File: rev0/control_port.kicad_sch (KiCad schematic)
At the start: 26 parts, among them IC1 ECP5-BGA256, U16 TC7USB42MU, U8 USB3343-CP

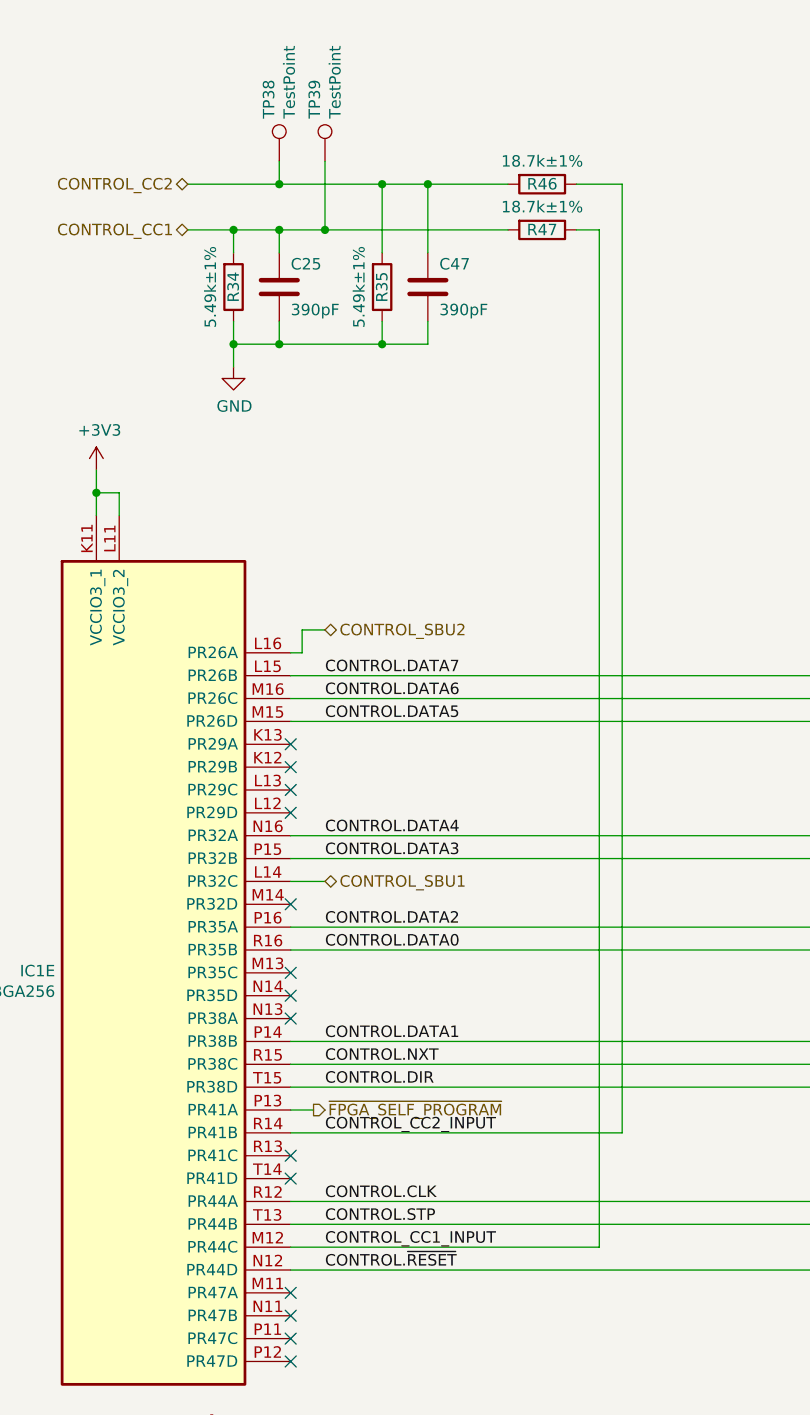
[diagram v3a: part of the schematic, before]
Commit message: hardware: simplify Control port Type-C connections
- remove CC/FPGA connections to ensure correct Rd is reliably present
- remove SBU/FPGA connections to avoid need for ESD protection

We provide CC and SBU pin access on the Target and Aux port. They are
not necessary on the Control port. Simplification ensures reliability.
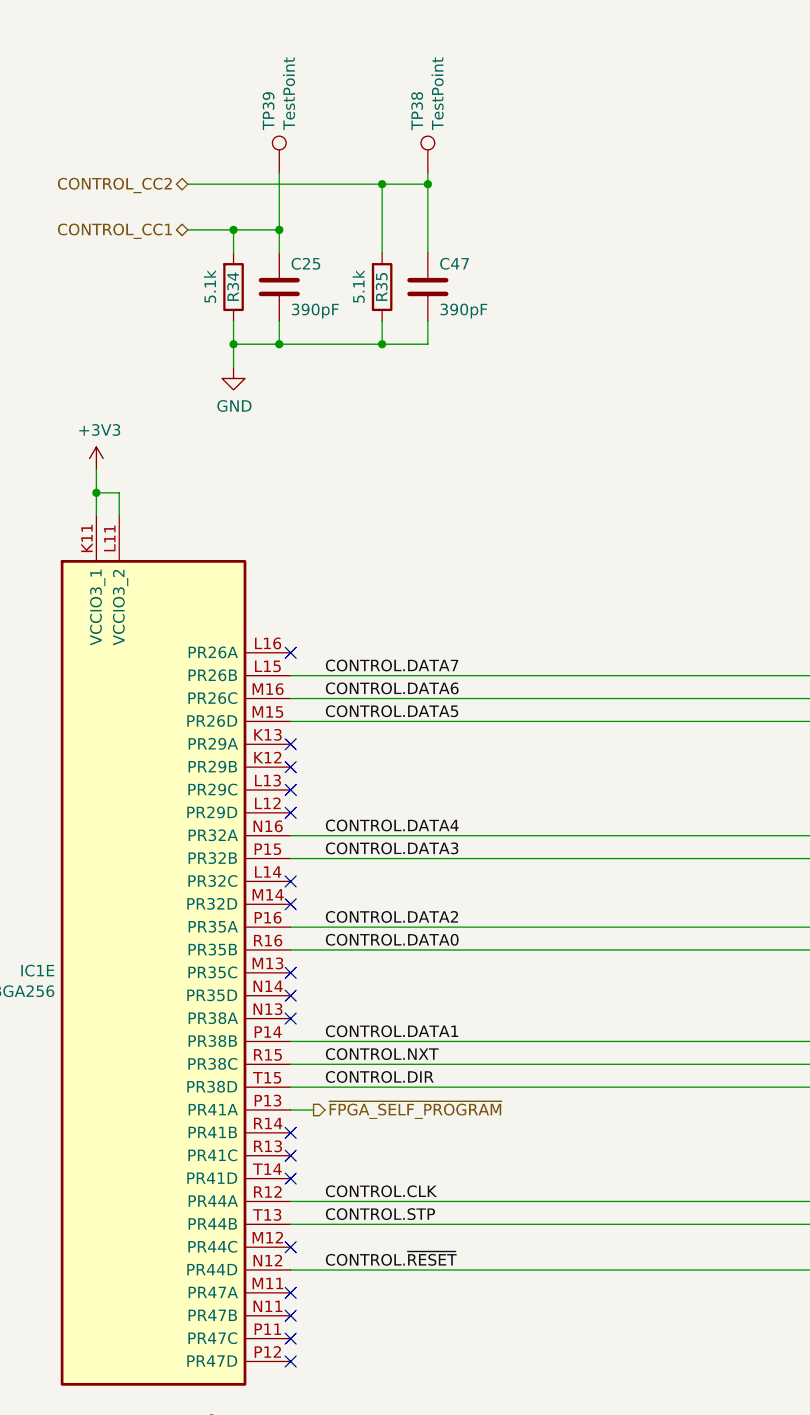
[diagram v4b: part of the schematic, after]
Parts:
- removed R46, R47: 18.7k±1%, Resistor_SMD:R_0402_1005Metric, symbol Device:R
- R34, R35: value 5.49k±1% -> 5.1k; Manufacturer Panasonic -> Yageo; Part Number ERJ-2RKF5491X -> RC0402JR-075K1L
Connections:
- net CONTROL_CC1_INPUT: no longer names the net of IC1.M12 (PR44C)
- net CONTROL_CC2_INPUT: no longer names the net of IC1.R14 (PR41B)
- net CONTROL_SBU1: no longer names the net of IC1.L14 (PR32C)
- net CONTROL_SBU2: no longer names the net of IC1.L16 (PR26A)
- no-connect marks 15 -> 19
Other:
- moved on the sheet: TP38, TP39

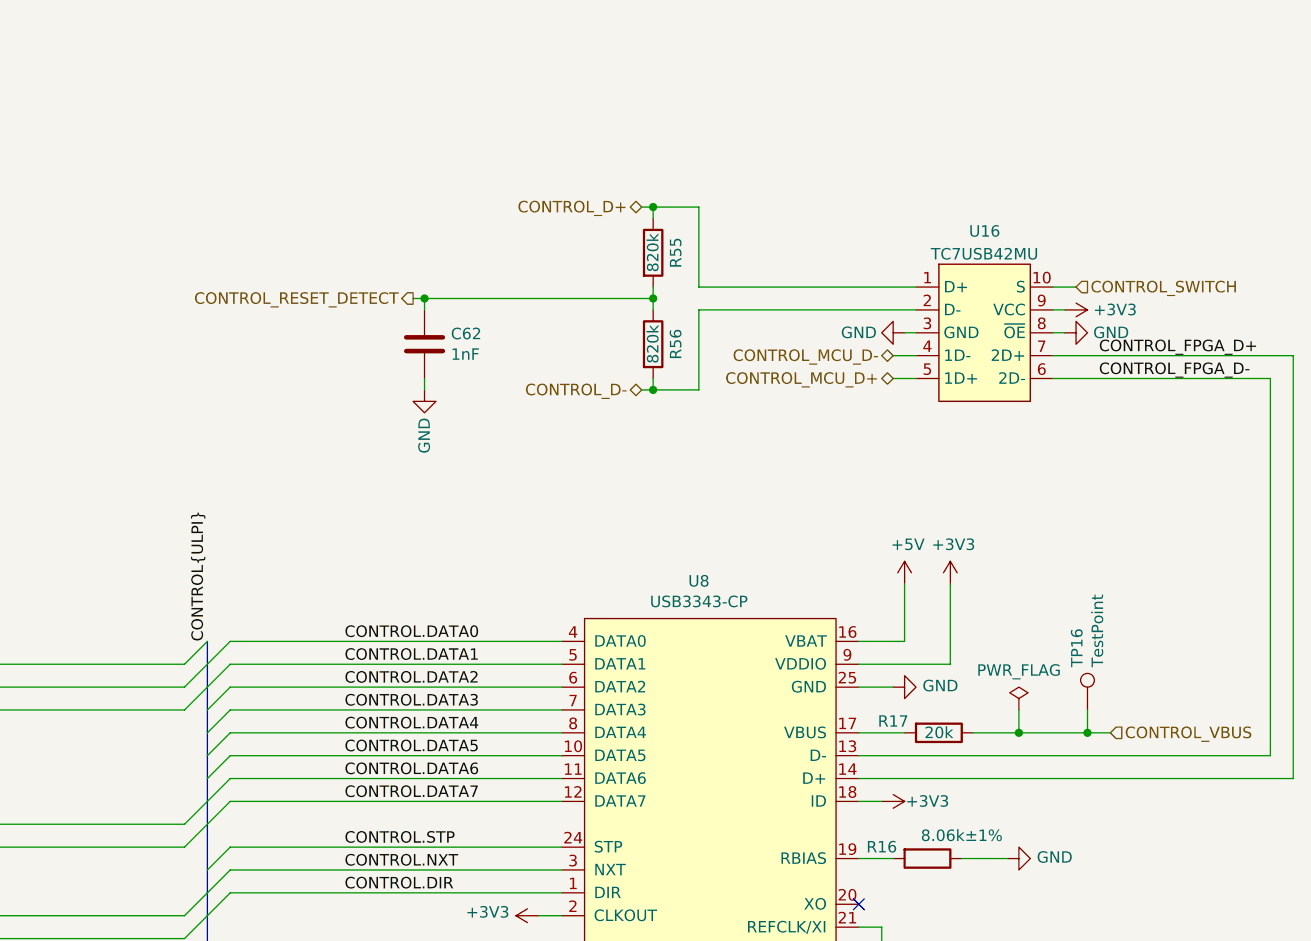
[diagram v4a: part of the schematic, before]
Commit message: hardware: clamp VBUS detection signals to 24 V
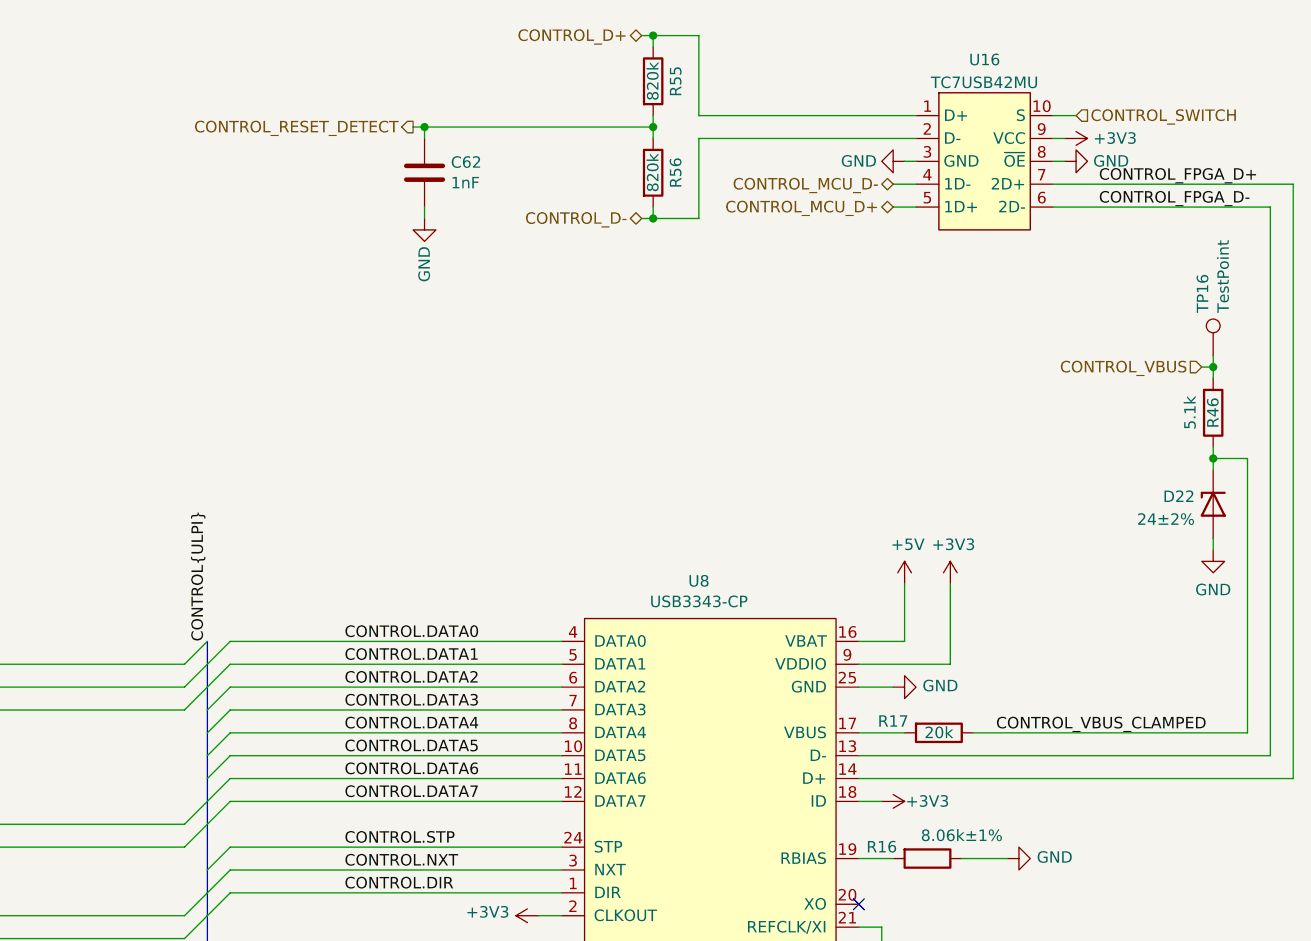
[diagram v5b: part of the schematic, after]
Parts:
- added D22: 24±2%, luna:DFN1006-2, symbol Device:D_Zener
- added R46: 5.1k, Resistor_SMD:R_0402_1005Metric, symbol Device:R
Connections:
- net CONTROL_VBUS: now also R46.2; no longer R17.1
- net GND: now also D22.2 (A)
- new net CONTROL_VBUS_CLAMPED: D22.1 (K), R17.1, R46.1
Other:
- moved on the sheet: C62, R55, R56, TP16, U16

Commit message: hardware: use "Exclude from bill of materials"
Virtual components such as mounting holes and test points that do not
require part placement now use this property instead of the DNP field.
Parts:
- TP15, TP16, TP17, TP2, TP38, TP39: DNP DNP -> (none); now left out of the parts list
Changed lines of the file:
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@@
   )
   (symbol (lib_id "Connector:TestPoint") (at 68.58 33.02 0) (unit 1)
-    (in_bom yes) (on_board yes)
+    (in_bom no) (on_board yes)
     (property "Reference" "TP38" (id 0) (at 67.437 28.2702 90)
       (effects (font (size 1.27 1.27)) (justify left))
@@
       (effects (font (size 1.27 1.27)) hide)
     )
-    (property "DNP" "DNP" (id 4) (at 68.58 33.02 0)
-      (effects (font (size 1.27 1.27)) hide)
-    )
     (pin "1")
   )
   (symbol (lib_id "Connector:TestPoint") (at 52.07 33.02 0) (unit 1)
-    (in_bom yes) (on_board yes)
+    (in_bom no) (on_board yes)
     (property "Reference" "TP39" (id 0) (at 50.927 28.2702 90)
       (effects (font (size 1.27 1.27)) (justify left))
@@
     )
     (property "Datasheet" "~" (id 3) (at 57.15 33.02 0)
-      (effects (font (size 1.27 1.27)) hide)
-    )
-    (property "DNP" "DNP" (id 4) (at 52.07 33.02 0)
       (effects (font (size 1.27 1.27)) hide)
     )
@@
   )
   (symbol (lib_id "Connector:TestPoint") (at 256.54 124.46 270) (unit 1)
-    (in_bom yes) (on_board yes)
+    (in_bom no) (on_board yes)
     (property "Reference" "TP17" (id 0) (at 261.2898 123.317 90)
       (effects (font (size 1.27 1.27)) (justify left))
@@
       (effects (font (size 1.27 1.27)) hide)
     )
-    (property "DNP" "DNP" (id 4) (at 256.54 124.46 0)
-      (effects (font (size 1.27 1.27)) hide)
-    )
     (pin "1")
   )
   (symbol (lib_id "Connector:TestPoint") (at 265.43 54.61 0) (unit 1)
-    (in_bom yes) (on_board yes)
+    (in_bom no) (on_board yes)
     (property "Reference" "TP16" (id 0) (at 264.287 49.8602 90)
       (effects (font (size 1.27 1.27)) (justify left))
@@
       (effects (font (size 1.27 1.27)) hide)
     )
-    (property "DNP" "DNP" (id 4) (at 265.43 54.61 0)
-      (effects (font (size 1.27 1.27)) hide)
-    )
     (pin "1")
   )
   (symbol (lib_id "Connector:TestPoint") (at 124.46 157.48 180) (unit 1)
-    (in_bom yes) (on_board yes)
+    (in_bom no) (on_board yes)
     (property "Reference" "TP15" (id 0) (at 125.603 162.2298 90)
       (effects (font (size 1.27 1.27)) (justify left))
@@
       (effects (font (size 1.27 1.27)) hide)
     )
-    (property "DNP" "DNP" (id 4) (at 124.46 157.48 0)
-      (effects (font (size 1.27 1.27)) hide)
-    )
     (pin "1")
   )
   (symbol (lib_id "Connector:TestPoint") (at 119.38 157.48 180) (unit 1)
-    (in_bom yes) (on_board yes)
+    (in_bom no) (on_board yes)
     (property "Reference" "TP2" (id 0) (at 120.523 162.2298 90)
       (effects (font (size 1.27 1.27)) (justify left))
@@
       (effects (font (size 1.27 1.27)) hide)
     )
-    (property "DNP" "DNP" (id 4) (at 119.38 157.48 0)
-      (effects (font (size 1.27 1.27)) hide)
-    )

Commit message: hardware: component placement
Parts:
- U16: value TC7USB42MU -> PI3USB102G; footprint (none) -> luna:Diodes_10-TQFN_ZL; Manufacturer Toshiba -> Diodes Inc.; Part Number TC7USB42MU,LF(S2E -> PI3USB102GZLEX
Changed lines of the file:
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@@
     (in_bom yes) (on_board yes) (fields_autoplaced)
     (property "Reference" "U16" (id 0) (at 240.03 21.751 0))
-    (property "Value" "TC7USB42MU" (id 1) (at 240.03 24.2879 0))
-    (property "Footprint" "" (id 2) (at 240.03 33.02 0)
+    (property "Value" "PI3USB102G" (id 1) (at 240.03 24.2879 0))
+    (property "Footprint" "luna:Diodes_10-TQFN_ZL" (id 2) (at 240.03 33.02 0)
       (effects (font (size 1.27 1.27)) hide)
     )
-    (property "Datasheet" "https://toshiba.semicon-storage.com/info/TC7USB42MU_datasheet_en_20200616.pdf?did=13905&prodName=TC7USB42MU" (id 3) (at 240.03 33.02 0)
+    (property "Datasheet" "https://www.diodes.com/assets/Datasheets/PI3USB102G.pdf" (id 3) (at 240.03 33.02 0)
       (effects (font (size 1.27 1.27)) hide)
     )
-    (property "Manufacturer" "Toshiba" (id 4) (at 240.03 33.02 0)
+    (property "Manufacturer" "Diodes Inc." (id 4) (at 240.03 33.02 0)
       (effects (font (size 1.27 1.27)) hide)
     )
-    (property "Part Number" "TC7USB42MU,LF(S2E" (id 5) (at 240.03 33.02 0)
+    (property "Part Number" "PI3USB102GZLEX" (id 5) (at 240.03 33.02 0)
       (effects (font (size 1.27 1.27)) hide)
     )
